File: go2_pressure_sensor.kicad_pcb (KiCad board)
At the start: 2 copper layers, 17.5 x 19.6 mm, 11 parts, among them J2 Conn_01x03_Socket, U3 XPGZP6859A, U4 LP2980-ADJ

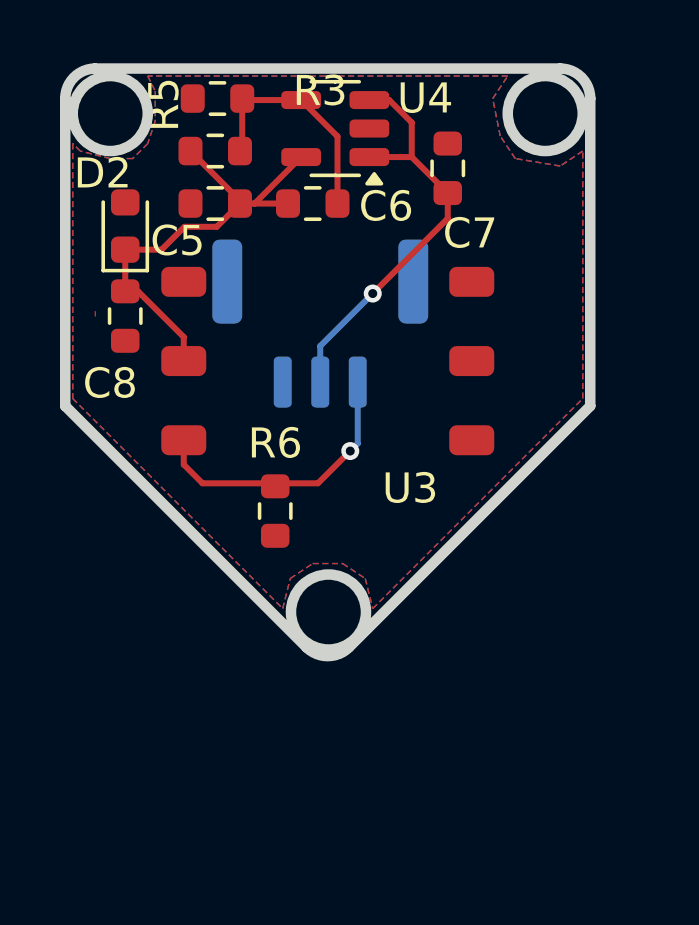
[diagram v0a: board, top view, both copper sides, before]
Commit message: Removed copied sensors schematic
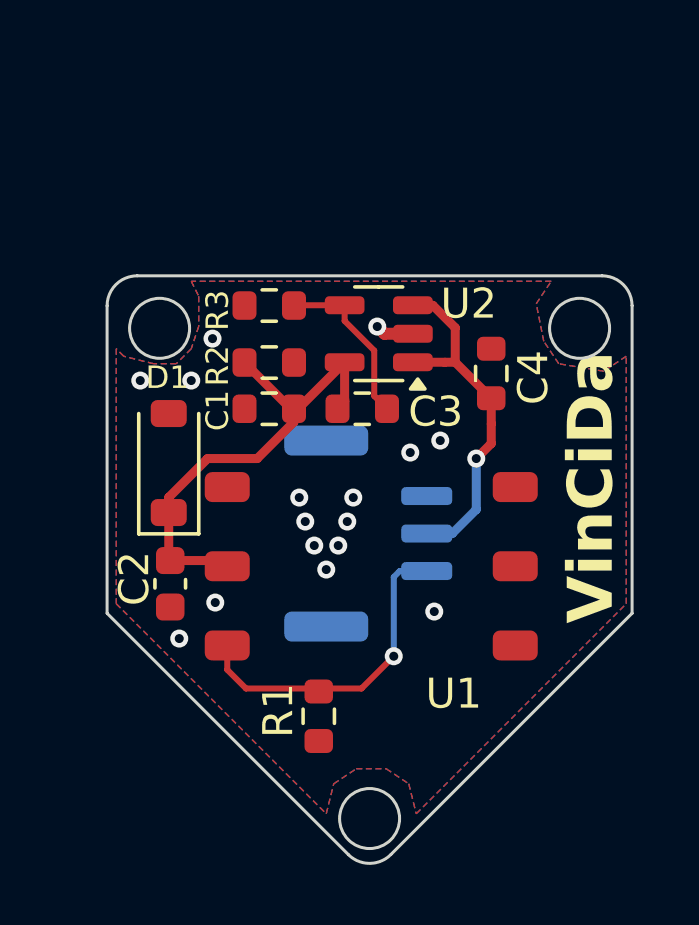
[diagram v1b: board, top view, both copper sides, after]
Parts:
- C2: renamed from C8; footprint Resistor_SMD:R_0603_1608Metric -> Capacitor_SMD:C_0603_1608Metric
- D1: renamed from D2; footprint Diode_SMD:D_0603_1608Metric -> Diode_SMD:D_SOD-123
- moved C2 9.05 mm to (61.0, 52.2)
- moved D1 8.03 mm to (61.0, 48.1)
- moved R2 7.28 mm to (64.3, 44.8)
- moved J1 7.18 mm to (67.6, 50.5), turned to -90 degrees
- moved R3 7.11 mm to (64.3, 42.9)
- moved C1 7.07 mm to (64.3, 46.3)
- moved C3 7.04 mm to (67.4, 46.3)
- moved R1 6.99 mm to (66.0, 56.6)
- moved U1 6.99 mm to (67.7, 51.6)
- moved U2 6.99 mm to (68.0, 43.8)
- moved C4 6.99 mm to (71.7, 45.2)
- renumbered C5 to C1, C6 to C3, C7 to C4, J2 to J1, R6 to R1, R3 to R2, R5 to R3, U3 to U1, U4 to U2
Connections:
- J1 pad 1: /OUT -> GND
- J1 pad 3: GND -> /OUT
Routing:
- net Net-(J1-Pin_2): track 14.0 -> 11.9 mm
- net Net-(U2-ADJ): track 7.72 -> 5.74 mm
- net /OUT: track 9.47 -> 11.0 mm
- net /VDD: track 15.0 -> 16.0 mm
- net GND: track 0.00 -> 0.81 mm, vias 0 -> 16
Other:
- outline, holes or cut-outs redrawn
- board text added: "The RoboVerse"
- board text added: "VinCiDa"

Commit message: Added silkscreen markings for pressure sensor
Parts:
- R2: value 90k -> 86.6k
- moved J1 1.90 mm to (67.6, 52.4)
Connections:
- U1 pad 6: unconnected-(U1-GND-Pad6) -> GND
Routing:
- net /OUT: track 11.0 -> 8.62 mm
- net Net-(U2-ADJ): track 5.74 -> 7.64 mm
- net Net-(J1-Pin_2): track 11.9 -> 13.8 mm
- net GND: vias 16 -> 20
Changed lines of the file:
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@@
 			(drillshape 0)
 			(scaleselection 1)
-			(outputdirectory "gerber/")
+			(outputdirectory "gerber/v3/")
 		)
 	)
@@
 	(net 6 "unconnected-(U1-NC-Pad4)")
 	(net 7 "unconnected-(U1-NC-Pad5)")
-	(net 8 "unconnected-(U1-GND-Pad6)")
-	(net 9 "unconnected-(U1-NC-Pad1)")
+	(net 8 "unconnected-(U1-NC-Pad1)")
 	(footprint "Package_TO_SOT_SMD:SOT-23-5"
 		(layer "F.Cu")
@@
 			)
 		)
-		(property "LCSC" "C5310801"
+		(property "LCSC" "C181526"
 			(at 0 0 180)
 			(unlocked yes)
@@
 			)
 		)
-		(property "Value" "90k"
+		(property "Value" "86.6k"
 			(at 0 1.43 0)
 			(layer "F.Fab")
@@
 			)
 		)
-		(property "LCSC" "C23129"
+		(property "LCSC" "C3000725"
 			(at 0 0 180)
 			(unlocked yes)
@@
 		(sheetfile "go2_pressure_sensor.kicad_sch")
 		(attr smd)
+		(fp_line
+			(start -0.6 -2.6)
+			(end -0.6 -3.6)
+			(stroke
+				(width 0.1)
+				(type default)
+			)
+			(layer "F.SilkS")
+		)
+		(fp_line
+			(start 0.6 -2.6)
+			(end 0.6 -3.6)
+			(stroke
+				(width 0.1)
+				(type default)
+			)
+			(layer "F.SilkS")
+		)
+		(fp_rect
+			(start -3.4 -3.6)
+			(end 3.5 3.5)
+			(stroke
+				(width 0.1)
+				(type default)
+			)
+			(fill none)
+			(layer "F.SilkS")
+		)
+		(fp_arc
+			(start 0.6 -2.6)
+			(mid 0 -2)
+			(end -0.6 -2.6)
+			(stroke
+				(width 0.1)
+				(type default)
+			)
+			(layer "F.SilkS")
+		)
+		(fp_circle
+			(center 0 0)
+			(end 0.8 -0.5)
+			(stroke
+				(width 0.1)
+				(type default)
+			)
+			(fill none)
+			(layer "F.SilkS")
+		)
 		(fp_text user "${REFERENCE}"
 			(at 0 1.5 0)
@@
 			(layers "F.Cu" "F.Paste" "F.Mask")
 			(roundrect_rratio 0.25)
-			(net 9 "unconnected-(U1-NC-Pad1)")
+			(net 8 "unconnected-(U1-NC-Pad1)")
 			(pinfunction "NC")
 			(pintype "no_connect")
@@
 			(layers "F.Cu" "F.Paste" "F.Mask")
 			(roundrect_rratio 0.25)
-			(net 8 "unconnected-(U1-GND-Pad6)")
+			(net 2 "GND")
 			(pinfunction "GND")
-			(pintype "no_connect")
+			(pintype "input")
 			(thermal_bridge_angle 45)
 		)
@@
 	(footprint "Connector_JST:JST_GH_BM03B-GHS-TBT_1x03-1MP_P1.25mm_Vertical"
 		(layer "B.Cu")
-		(at 67.6 50.5 -90)
+		(at 67.6 52.4 -90)
 		(descr "JST GH series connector, BM03B-GHS-TBT (http://www.jst-mfg.com/product/pdf/eng/eGH.pdf), generated with kicad-footprint-generator")
 		(tags "connector JST GH vertical")
@@
 	)
 	(segment
-		(start 68.65 51.75)
-		(end 69.55 51.75)
-		(width 0.2)
-		(layer "B.Cu")
-		(net 1)
-	)
-	(segment
 		(start 68.4 54.54)
 		(end 68.45 54.59)
@@
 	)
 	(segment
-		(start 68.45 51.95)
-		(end 68.65 51.75)
+		(start 69.39 53.65)
+		(end 68.45 54.59)
 		(width 0.2)
 		(layer "B.Cu")
@@
 	)
 	(segment
-		(start 68.45 54.59)
-		(end 68.45 51.95)
+		(start 69.55 53.65)
+		(end 69.39 53.65)
 		(width 0.2)
 		(layer "B.Cu")
@@
 	)
 	(via
+		(at 73.4 47.3)
+		(size 0.6)
+		(drill 0.3)
+		(layers "F.Cu" "B.Cu")
+		(net 2)
+	)
+	(via
 		(at 69 47.8)
 		(size 0.6)
@@
 	)
 	(via
-		(at 67.1 49.3)
+		(at 67.1 51)
+		(size 0.6)
+		(drill 0.3)
+		(layers "F.Cu" "B.Cu")
+		(net 2)
+	)
+	(via
+		(at 75 49)
 		(size 0.6)
 		(drill 0.3)
@@
 	)
 	(via
-		(at 69.8 53.1)
+		(at 66.9 51.8)
 		(size 0.6)
 		(drill 0.3)
@@
 	)
 	(via
-		(at 66.9 50.1)
+		(at 66.2 53.4)
 		(size 0.6)
 		(drill 0.3)
@@
 	)
 	(via
-		(at 66.2 51.7)
+		(at 73.7 50.4)
 		(size 0.6)
 		(drill 0.3)
@@
 	)
 	(via
-		(at 65.5 50.1)
+		(at 65.5 51.8)
+		(size 0.6)
+		(drill 0.3)
+		(layers "F.Cu" "B.Cu")
+		(net 2)
+	)
+	(via
+		(at 65.3 51)
 		(size 0.6)
 		(drill 0.3)
@@
 	)
 	(via
-		(at 65.3 49.3)
+		(at 72.5 50.4)
 		(size 0.6)
 		(drill 0.3)
@@
 	)
 	(via
-		(at 65.8 50.9)
+		(at 65.8 52.6)
 		(size 0.6)
 		(drill 0.3)
@@
 	)
 	(via
-		(at 66.6 50.9)
+		(at 66.6 52.6)
+		(size 0.6)
+		(drill 0.3)
+		(layers "F.Cu" "B.Cu")
+		(net 2)
+	)
+	(via
+		(at 72.6 47.3)
 		(size 0.6)
 		(drill 0.3)
@@
 	)
 	(segment
+		(start 65.125 44.8)
+		(end 65.125 42.9)
+		(width 0.2)
+		(layer "F.Cu")
+		(net 3)
+	)
+	(segment
 		(start 68.225 46.34)
 		(end 67.8 45.915)
@@
 	)
 	(segment
-		(start 70.399999 50.5)
-		(end 69.55 50.5)
-		(width 0.3)
+		(start 70.399999 52.4)
+		(end 71.2 51.599999)
+		(width 0.2)
 		(layer "B.Cu")
 		(net 5)
 	)
 	(segment
-		(start 71.2 48)
-		(end 71.2 49.699999)
-		(width 0.3)
+		(start 69.55 52.4)
+		(end 70.399999 52.4)
+		(width 0.2)
 		(layer "B.Cu")
 		(net 5)
 	)
 	(segment
-		(start 71.2 49.699999)
-		(end 70.399999 50.5)
-		(width 0.3)
+		(start 71.2 51.599999)
+		(end 71.2 48)
+		(width 0.2)
 		(layer "B.Cu")
 		(net 5)
